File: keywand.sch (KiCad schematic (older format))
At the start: 30 parts

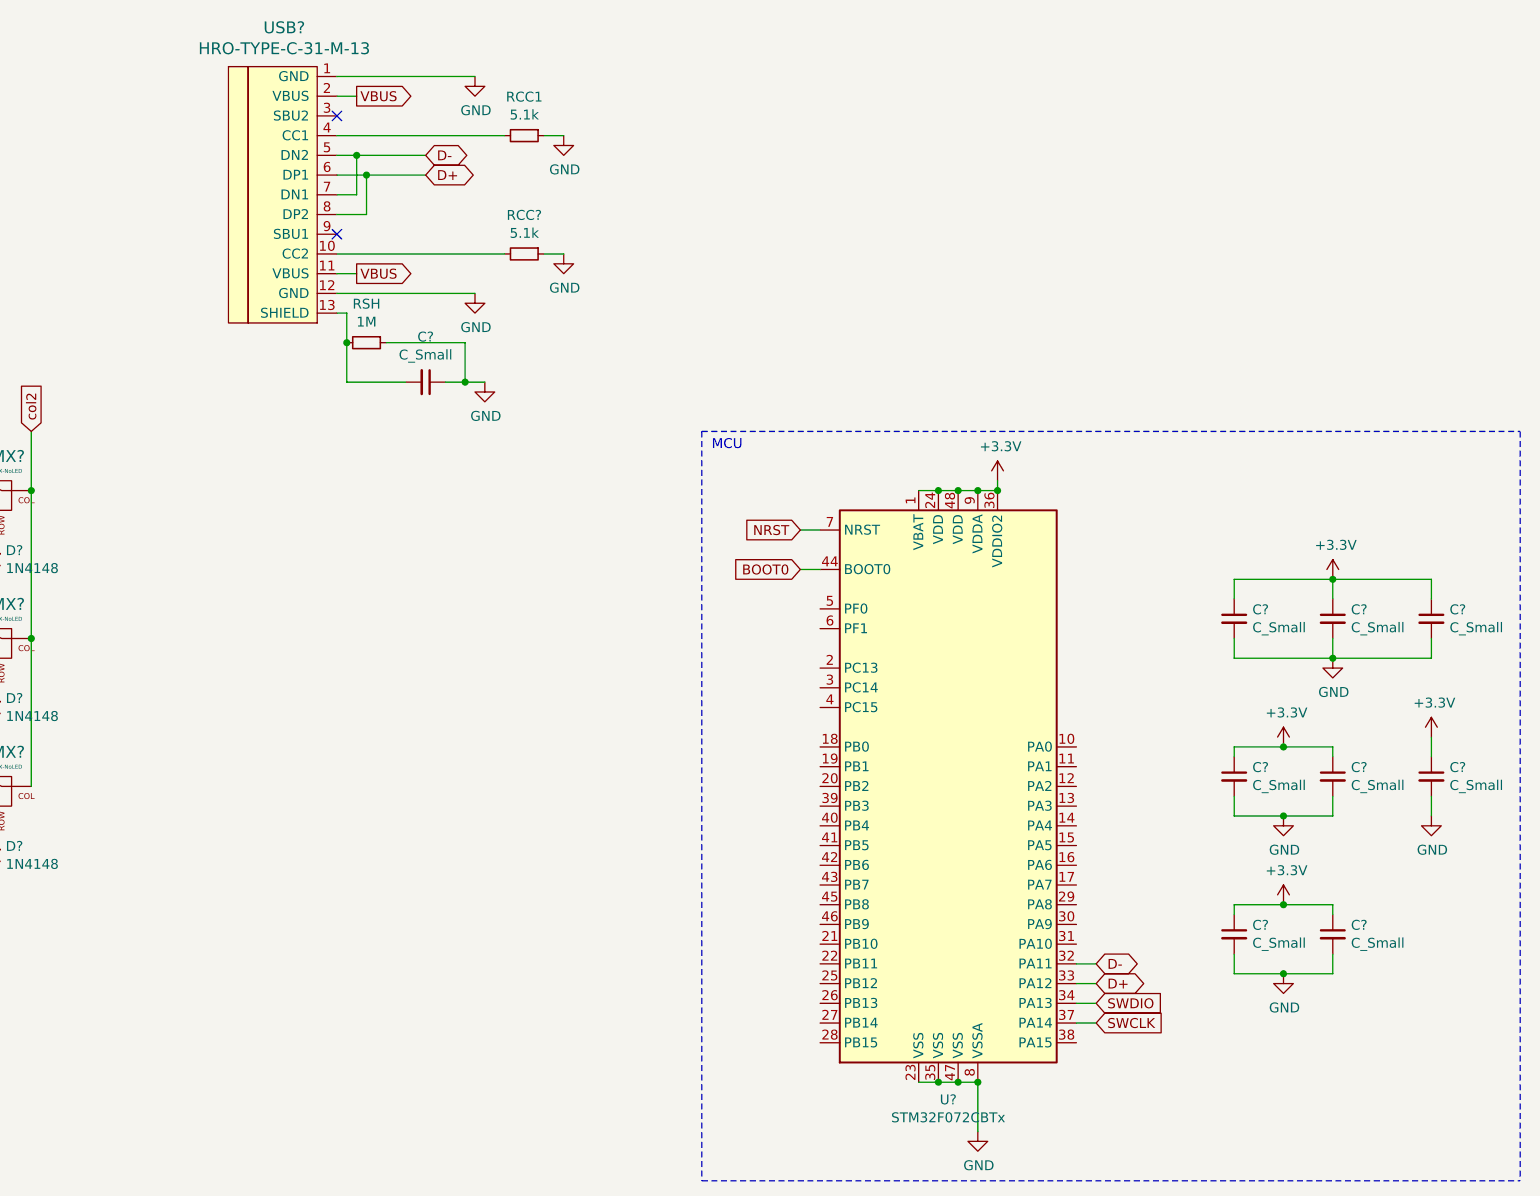
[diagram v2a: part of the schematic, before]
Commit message: Added rgb underglow
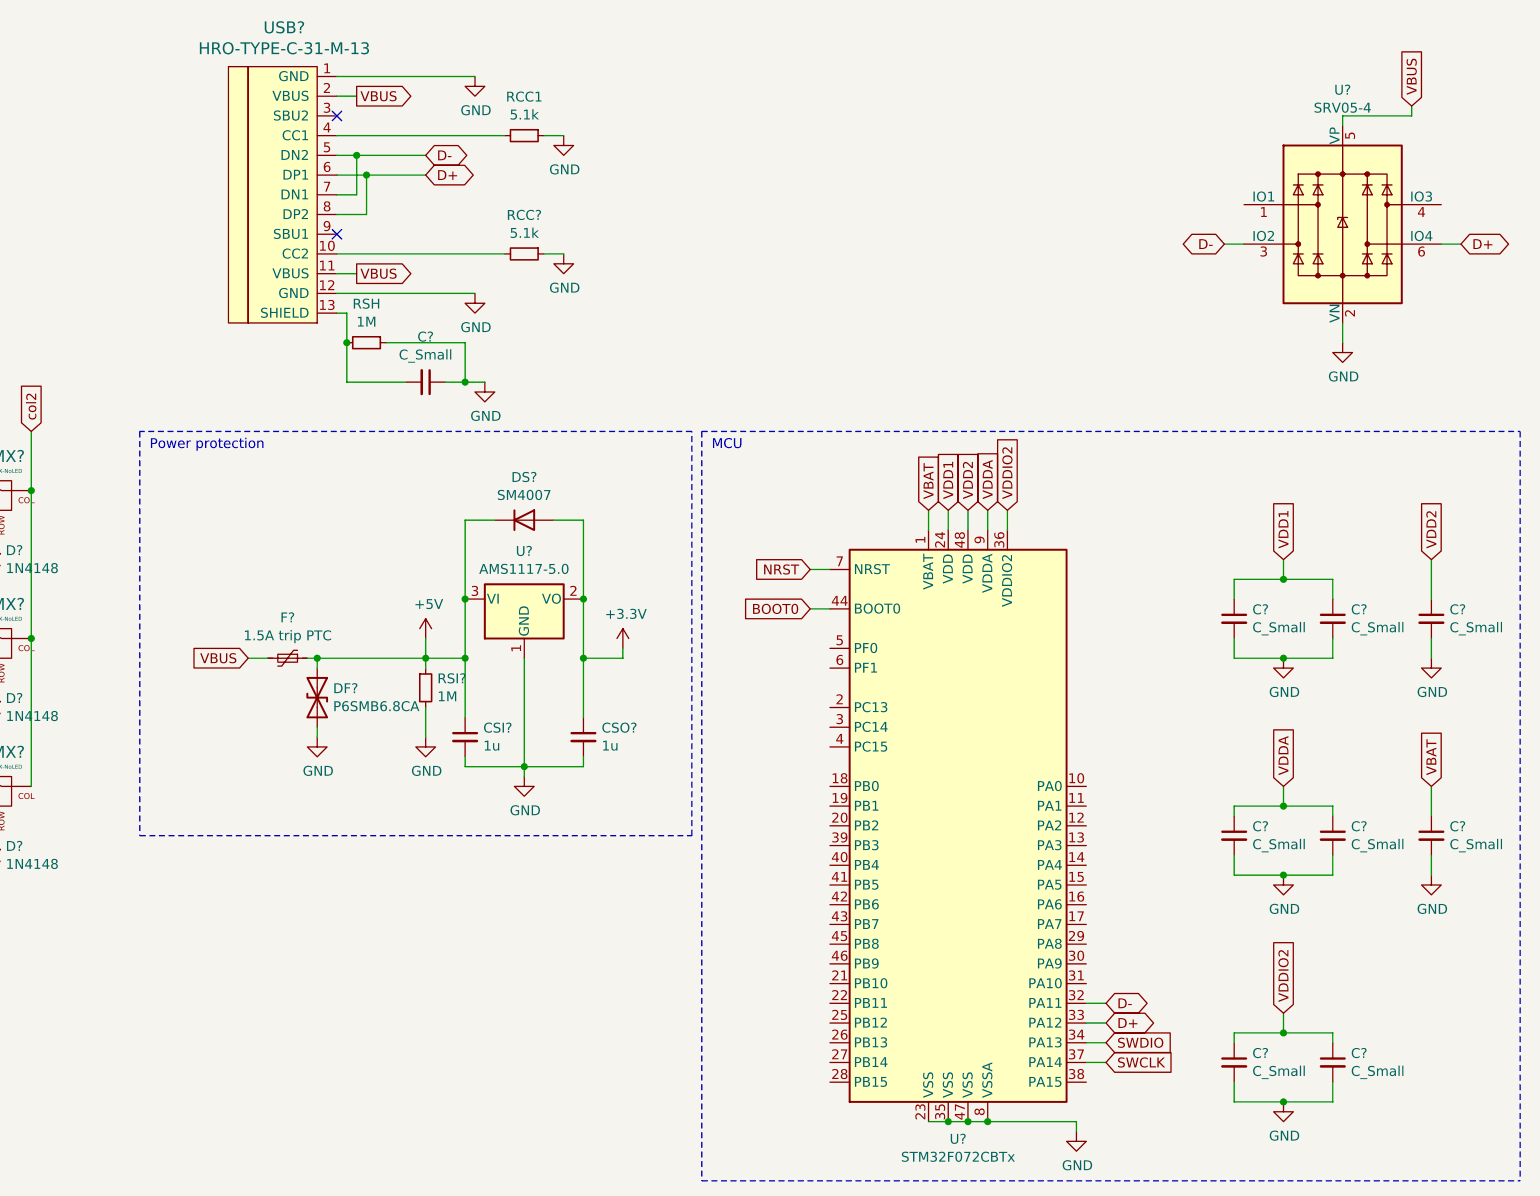
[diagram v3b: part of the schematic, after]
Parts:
- added CSI?, CSO?: 1u, Capacitor_SMD:C_0805_2012Metric, symbol Device:C_Small
- added DF?: P6SMB6.8CA, Diode_SMD:D_SMB, symbol Device:D_TVS
- added DS?: SM4007, Diode_SMD:D_MELF, symbol Diode:SM4007
- added F?: 1.5A trip PTC, Fuse:Fuse_1812_4532Metric, symbol Device:Polyfuse_Small
- added RSI?: 1M, Capacitor_SMD:C_0805_2012Metric, symbol Device:R_Small
- added U?: AMS1117-5.0, Package_TO_SOT_SMD:SOT-223-3_TabPin2, symbol Regulator_Linear:AMS1117-5.0
- added U?: SRV05-4, Package_TO_SOT_SMD:SOT-23-6, symbol Power_Protection:SRV05-4
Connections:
- net +3V3: now also CSO?.1, DS?.2 (A), U?.2 (VO); no longer C?.1, C?.1, C?.1, C?.1, C?.1, C?.1, C?.1, C?.1, U?.1 (VBAT), U?.24 (VDD), U?.36 (VDDIO2), U?.48 (VDD), U?.9 (VDDA)
- net D+: now also U?.6 (IO4)
- net D-: now also U?.3 (IO2)
- net GND: now also CSI?.2, CSO?.2, DF?.2 (A2), RSI?.2, U?.1 (GND), U?.2 (VN)
- net VBUS: now also F?.2, U?.5 (VP)
- new net +5V: CSI?.1, DF?.1 (A1), DS?.1 (K), F?.1, RSI?.1, U?.3 (VI)
- new net VBAT: C?.1, U?.1 (VBAT)
- new net VDD1: C?.1, C?.1, U?.24 (VDD)
- new net VDD2: C?.1, U?.48 (VDD)
- new net VDDA: C?.1, C?.1, U?.9 (VDDA)
- new net VDDIO2: C?.1, C?.1, U?.36 (VDDIO2)
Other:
- note added: "Power protection"
- moved on the sheet: C?, U?

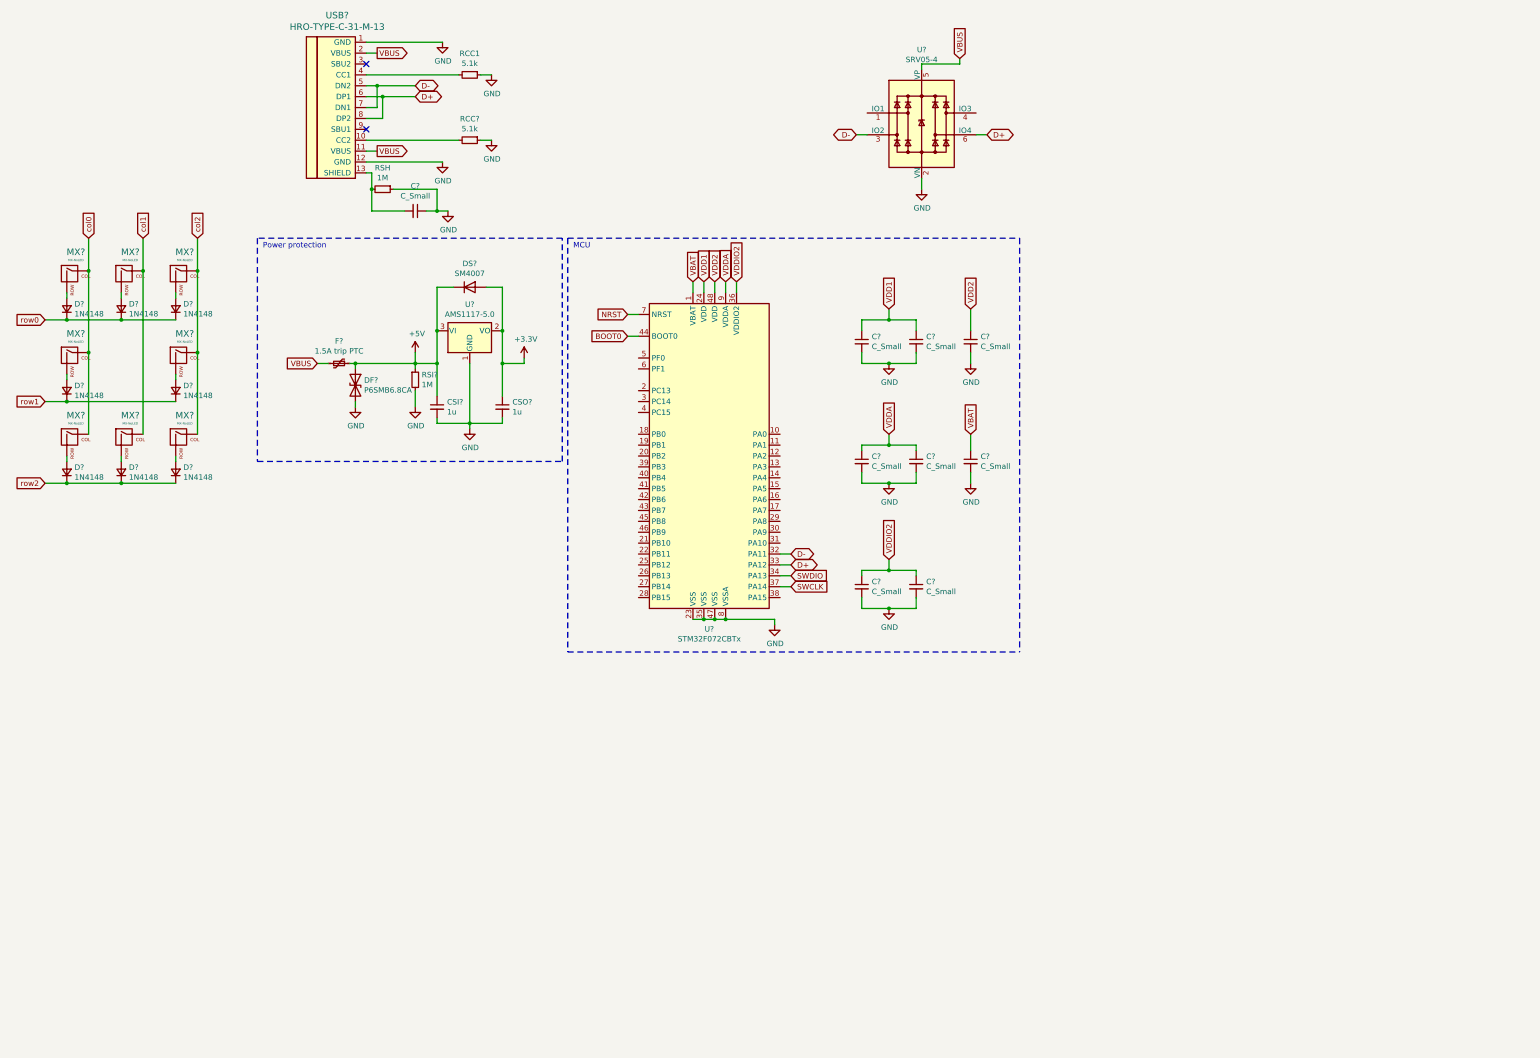
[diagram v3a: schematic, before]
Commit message: Started layout of board!
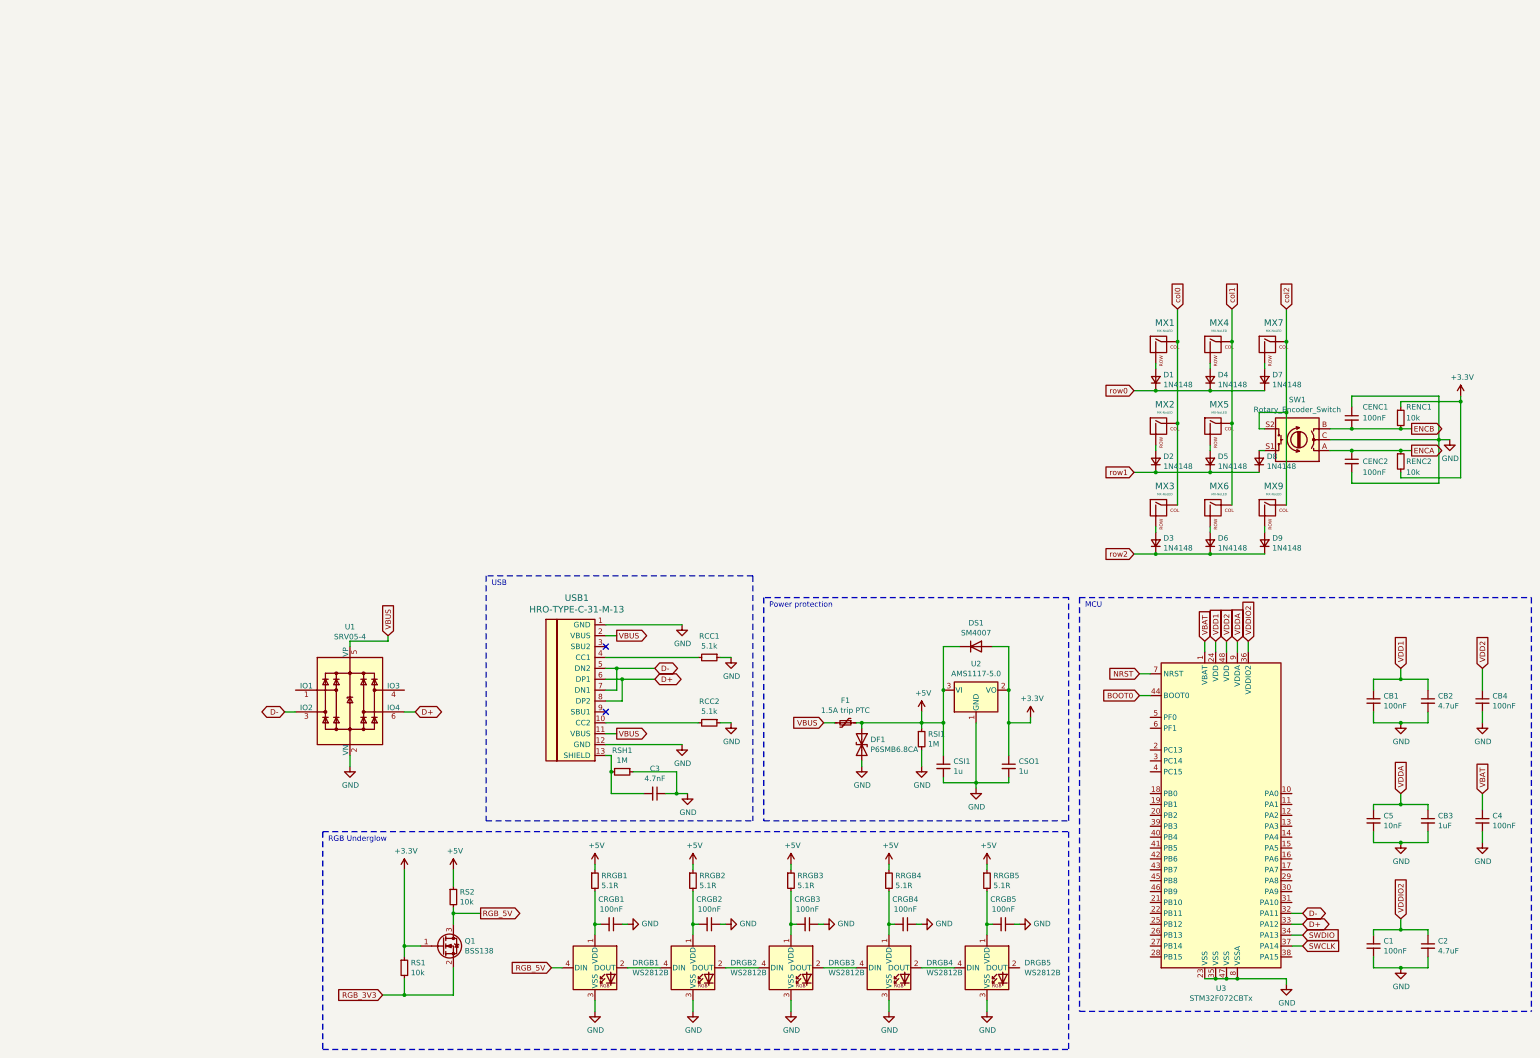
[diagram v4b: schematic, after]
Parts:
- removed C? (x6): C_Small, symbol Device:C_Small
- added C1, C4, CB1, CB4: 100nF, Capacitor_SMD:C_0402_1005Metric, symbol Device:C_Small
- added C2, CB2: 4.7uF, Capacitor_SMD:C_0402_1005Metric, symbol Device:C_Small
- added CENC1, CENC2, CRGB1, CRGB2, CRGB3, CRGB4, CRGB5: 100nF, Capacitor_SMD:C_0603_1608Metric, symbol Device:C_Small
- added D8: 1N4148, Diode_SMD:D_SOD-123, symbol Device:D_Small
- added DRGB1, DRGB2, DRGB3, DRGB4, DRGB5: WS2812B, LED_SMD:LED_SK6812MINI_PLCC4_3.5x3.5mm_P1.75mm, symbol LED:WS2812B
- added Q1: BSS138, Package_TO_SOT_SMD:SOT-23, symbol Transistor_FET:BSS138
- added RENC1, RENC2: 10k, Capacitor_SMD:C_0603_1608Metric, symbol Device:R_Small
- added RRGB1, RRGB2, RRGB3, RRGB4, RRGB5: 5.1R, Resistor_SMD:R_0603_1608Metric, symbol Device:R_Small
- added RS1, RS2: 10k, Resistor_SMD:R_1206_3216Metric, symbol Device:R_Small
- added SW1: Rotary_Encoder_Switch, Rotary_Encoder:RotaryEncoder_Alps_EC12E-Switch_Vertical_H20mm, symbol Device:Rotary_Encoder_Switch
- C3: renamed from C?; value C_Small -> 4.7nF; footprint (none) -> Capacitor_SMD:C_0603_1608Metric; LCSC (none) -> C53987
- C5: renamed from C?; value C_Small -> 10nF; footprint (none) -> Capacitor_SMD:C_0402_1005Metric; LCSC (none) -> C15195
- CB3: renamed from C?; value C_Small -> 1uF; footprint (none) -> Capacitor_SMD:C_0402_1005Metric; LCSC (none) -> C52923
- D1, D2, D3, D4, D5, D6, D7, D9: renamed from D?; footprint (none) -> Diode_SMD:D_SOD-123; LCSC (none) -> C81598
- MX1, MX2, MX3, MX4, MX5, MX6, MX7, MX9: renamed from MX?; footprint (none) -> MX_Only:MXOnly-1U-NoLED
- RCC1: footprint Resistor_SMD:R_0805_2012Metric -> Resistor_SMD:R_0603_1608Metric; Field4 C27834 -> C23186
- RCC2: renamed from RCC?; footprint Resistor_SMD:R_0805_2012Metric -> Resistor_SMD:R_0603_1608Metric; Field4 C27834 -> C23186
- RSH1: renamed from RSH; footprint Resistor_SMD:R_0805_2012Metric -> Resistor_SMD:R_0603_1608Metric; Field4 C17514 -> C22935
- RSI1: renamed from RSI?; footprint Capacitor_SMD:C_0805_2012Metric -> Capacitor_SMD:C_0603_1608Metric; JLCCode C17514 -> C22935
- gave numbers to parts that had none: 9
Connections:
- net +3V3: now also Q1.1 (G), RENC1.1, RENC2.2, RS1.1
- net +5V: now also RRGB1.1, RRGB2.1, RRGB3.1, RRGB4.1, RRGB5.1, RS2.1
- net GND: now also C1.2, C2.2, C4.2, CB1.2, CB2.2, CB4.2, CENC1.1, CENC2.2, CRGB1.1, CRGB2.1, CRGB3.1, CRGB4.1, CRGB5.1, DRGB1.3 (VSS), DRGB2.3 (VSS), DRGB3.3 (VSS), DRGB4.3 (VSS), DRGB5.3 (VSS), SW1.C
- net VBAT: now also C4.1
- net VDD1: now also CB1.1, CB2.1
- net VDD2: now also CB4.1
- net VDDIO2: now also C1.1, C2.1
- net col1: now also MX5.1 (COL)
- net col2: now also SW1.S2; no longer MX5.1 (COL)
- net row1: now also D8.1 (K)
- new net: CRGB5.2, DRGB5.1 (VDD), RRGB5.2
- new net: DRGB4.2 (DOUT), DRGB5.4 (DIN)
- new net: D8.2 (A), SW1.S1
- new net: CRGB4.2, DRGB4.1 (VDD), RRGB4.2
- new net: DRGB3.2 (DOUT), DRGB4.4 (DIN)
- new net: CRGB3.2, DRGB3.1 (VDD), RRGB3.2
- new net: DRGB2.2 (DOUT), DRGB3.4 (DIN)
- new net: CRGB2.2, DRGB2.1 (VDD), RRGB2.2
- new net: DRGB1.2 (DOUT), DRGB2.4 (DIN)
- new net: CRGB1.2, DRGB1.1 (VDD), RRGB1.2
- new net ENCA: CENC2.1, RENC2.1, SW1.A
- new net ENCB: CENC1.2, RENC1.2, SW1.B
- new net RGB_3V3: Q1.2 (S), RS1.2
- new net RGB_5V: DRGB1.4 (DIN), Q1.3 (D), RS2.2
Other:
- note added: "RGB Underglow"
- note added: "USB"
- moved on the sheet: C3, C5, CB3, CSI1, CSO1, D1, D2, D3, D4, D5, D6, D7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
